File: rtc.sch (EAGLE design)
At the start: 14 parts, among them U1 MCP79412, Y1 32.768 kHz

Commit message: v1.0
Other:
- note added: "CC BY-SA"
- note added: "Jack Christensen"
- note added: "MCP79412 Breakout Board"
- note added: "MCP79412 Breakout Board by Jack Christensen is licensed under"
- note added: "a Creative Commons Attribution-ShareAlike 3.0 Unported License."
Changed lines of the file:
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@@
 <layer number="209" name="209bmp" color="7" fill="1" visible="yes" active="yes"/>
 <layer number="210" name="210bmp" color="7" fill="1" visible="yes" active="yes"/>
+<layer number="211" name="211bmp" color="7" fill="1" visible="yes" active="yes"/>
+<layer number="212" name="212bmp" color="7" fill="1" visible="yes" active="yes"/>
+<layer number="213" name="213bmp" color="7" fill="1" visible="yes" active="yes"/>
+<layer number="214" name="214bmp" color="7" fill="1" visible="yes" active="yes"/>
+<layer number="215" name="215bmp" color="7" fill="1" visible="yes" active="yes"/>
+<layer number="216" name="216bmp" color="7" fill="1" visible="yes" active="yes"/>
 <layer number="250" name="Descript" color="7" fill="1" visible="no" active="no"/>
 <layer number="251" name="SMDround" color="7" fill="1" visible="no" active="no"/>
@@
 <sheet>
 <plain>
+<text x="10.16" y="15.24" size="2.1844" layer="91" ratio="10">MCP79412 Breakout Board by Jack Christensen is licensed under</text>
+<text x="10.16" y="20.32" size="4.572" layer="91" ratio="12">CC BY-SA</text>
+<text x="10.16" y="10.16" size="2.1844" layer="91" ratio="10">a Creative Commons Attribution-ShareAlike 3.0 Unported License.</text>
+<text x="149.86" y="30.48" size="3.048" layer="91" ratio="12">MCP79412 Breakout Board</text>
+<text x="149.86" y="25.4" size="3.048" layer="91" ratio="12">Jack Christensen</text>
 </plain>
 <instances>

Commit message: v1.1 Larger pads for D1.
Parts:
- D1: device zetex:DSOD323 -> _jc:DIODESOD-323F
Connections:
- net N$1: now also D1.K; no longer D1.C
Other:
- note added: "v1.1"
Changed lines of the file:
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@@
 <layer number="109" name="fp9" color="7" fill="1" visible="yes" active="yes"/>
 <layer number="110" name="fp0" color="7" fill="1" visible="yes" active="yes"/>
+<layer number="111" name="LPC17xx" color="7" fill="1" visible="yes" active="yes"/>
+<layer number="112" name="tSilk" color="7" fill="1" visible="yes" active="yes"/>
 <layer number="116" name="Patch_BOT" color="9" fill="4" visible="yes" active="yes"/>
 <layer number="121" name="_tsilk" color="7" fill="1" visible="yes" active="yes"/>
@@
 <layer number="123" name="tTestmark" color="7" fill="1" visible="yes" active="yes"/>
 <layer number="124" name="bTestmark" color="7" fill="1" visible="yes" active="yes"/>
+<layer number="125" name="_tNames" color="7" fill="1" visible="yes" active="yes"/>
+<layer number="126" name="_bNames" color="7" fill="1" visible="yes" active="yes"/>
+<layer number="127" name="_tValues" color="7" fill="1" visible="yes" active="yes"/>
+<layer number="128" name="_bValues" color="7" fill="1" visible="yes" active="yes"/>
 <layer number="131" name="tAdjust" color="7" fill="1" visible="yes" active="yes"/>
 <layer number="132" name="bAdjust" color="7" fill="1" visible="yes" active="yes"/>
 <layer number="144" name="Drill_legend" color="7" fill="1" visible="yes" active="yes"/>
 <layer number="151" name="HeatSink" color="7" fill="1" visible="yes" active="yes"/>
+<layer number="152" name="_bDocu" color="7" fill="1" visible="yes" active="yes"/>
 <layer number="199" name="Contour" color="7" fill="1" visible="yes" active="yes"/>
 <layer number="200" name="200bmp" color="1" fill="10" visible="no" active="no"/>
@@
 <layer number="215" name="215bmp" color="7" fill="1" visible="yes" active="yes"/>
 <layer number="216" name="216bmp" color="7" fill="1" visible="yes" active="yes"/>
+<layer number="217" name="217bmp" color="7" fill="1" visible="yes" active="yes"/>
+<layer number="218" name="218bmp" color="7" fill="1" visible="yes" active="yes"/>
+<layer number="219" name="219bmp" color="7" fill="1" visible="yes" active="yes"/>
+<layer number="220" name="220bmp" color="7" fill="1" visible="yes" active="yes"/>
+<layer number="221" name="221bmp" color="7" fill="1" visible="yes" active="yes"/>
+<layer number="222" name="222bmp" color="7" fill="1" visible="yes" active="yes"/>
+<layer number="223" name="223bmp" color="7" fill="1" visible="yes" active="yes"/>
+<layer number="224" name="224bmp" color="7" fill="1" visible="yes" active="yes"/>
+<layer number="248" name="Housing" color="7" fill="1" visible="yes" active="yes"/>
+<layer number="249" name="Edge" color="7" fill="1" visible="yes" active="yes"/>
 <layer number="250" name="Descript" color="7" fill="1" visible="no" active="no"/>
 <layer number="251" name="SMDround" color="7" fill="1" visible="no" active="no"/>
@@
 <part name="GND5" library="supply1" deviceset="GND" device=""/>
 <part name="P+2" library="supply1" deviceset="VCC" device=""/>
-<part name="D1" library="zetex" deviceset="D" device="SOD323" value="PMEG6002EJ"/>
+<part name="D1" library="_jc" deviceset="DIODE" device="SOD-323F" value="PMEG6002EJ"/>
 <part name="B1" library="_jc" deviceset="COIN-CELL" device="-2016-SMT" value="CR2016"/>
 <part name="GND6" library="supply1" deviceset="GND" device=""/>
@@
 <text x="149.86" y="30.48" size="3.048" layer="91" ratio="12">MCP79412 Breakout Board</text>
 <text x="149.86" y="25.4" size="3.048" layer="91" ratio="12">Jack Christensen</text>
+<text x="236.22" y="7.62" size="3.048" layer="91" ratio="12">v1.1</text>
 </plain>
 <instances>
@@
 <segment>
 <pinref part="R4" gate="G$1" pin="2"/>
-<pinref part="D1" gate="G$1" pin="C"/>
+<pinref part="D1" gate="G$1" pin="K"/>
 <wire x1="81.28" y1="83.82" x2="78.74" y2="83.82" width="0.1524" layer="91"/>
 </segment>

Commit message: Updated coin cell footprint, R and C footprints, OSHW logo.
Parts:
- added LOGO2: OSHW_LOGO_8MILX0150-NT, ohw-logo:OSHW_LOGO_8MILX0150-NT
- C1, C2, C3, C4: device rcl:C-USC0805 -> _jc:C-USM0805
- R1, R2, R3, R4: device rcl:R-US_R0805 -> _jc:R-US_M0805
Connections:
- net BAT: now also B1.POS1, B1.POS2; no longer B1.B+
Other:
- note added: "v1.2"
- note removed: "v1.1"
- moved on the sheet: C2, C3, C4, D1, R4, Y1

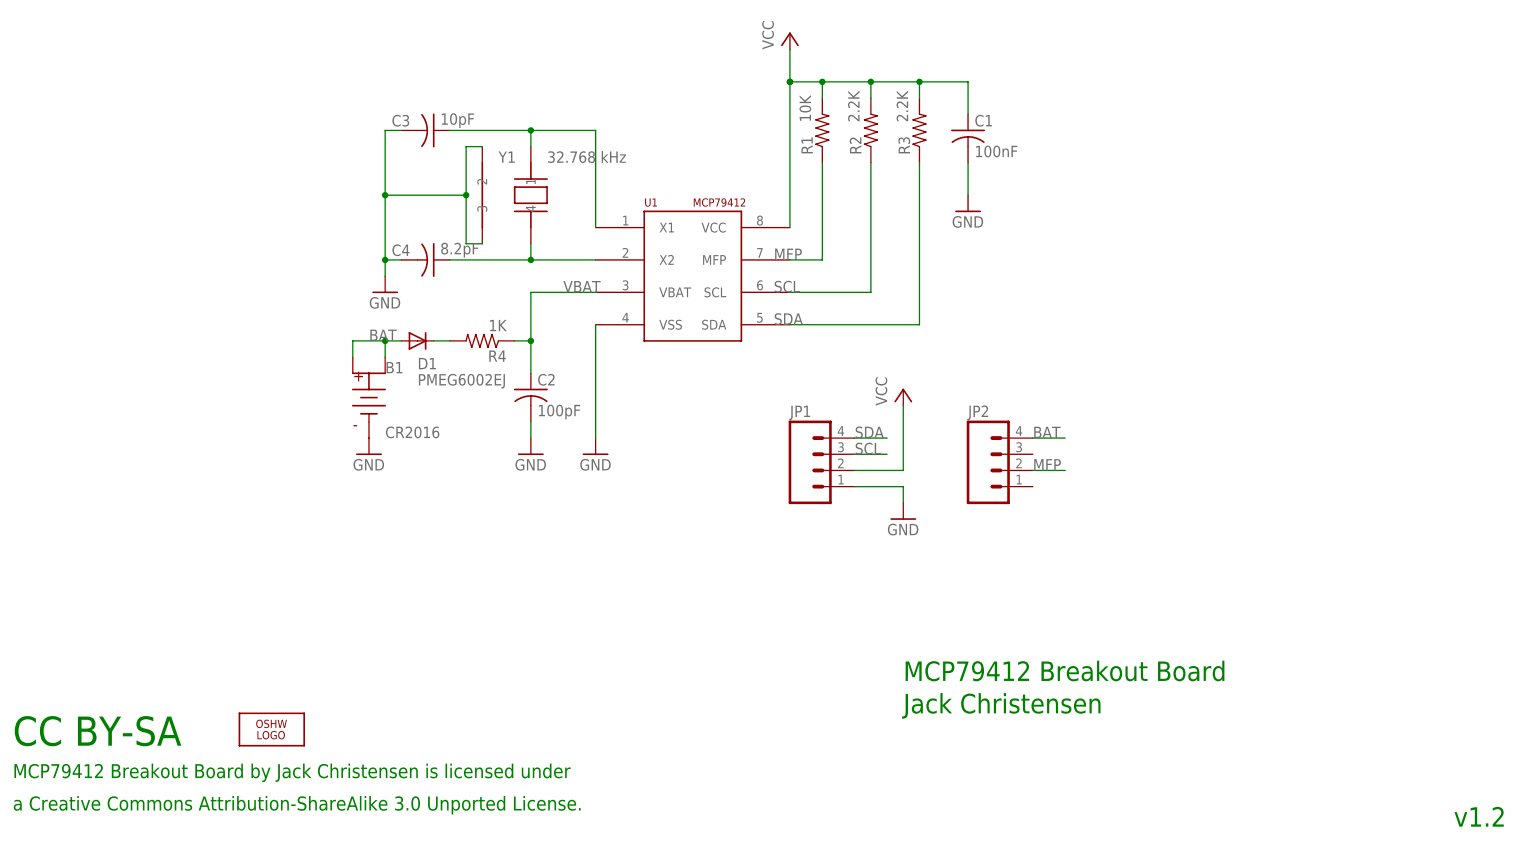
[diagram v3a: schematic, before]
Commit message: Update README, add LICENSE and other misc files. Regenerate Gerber files.
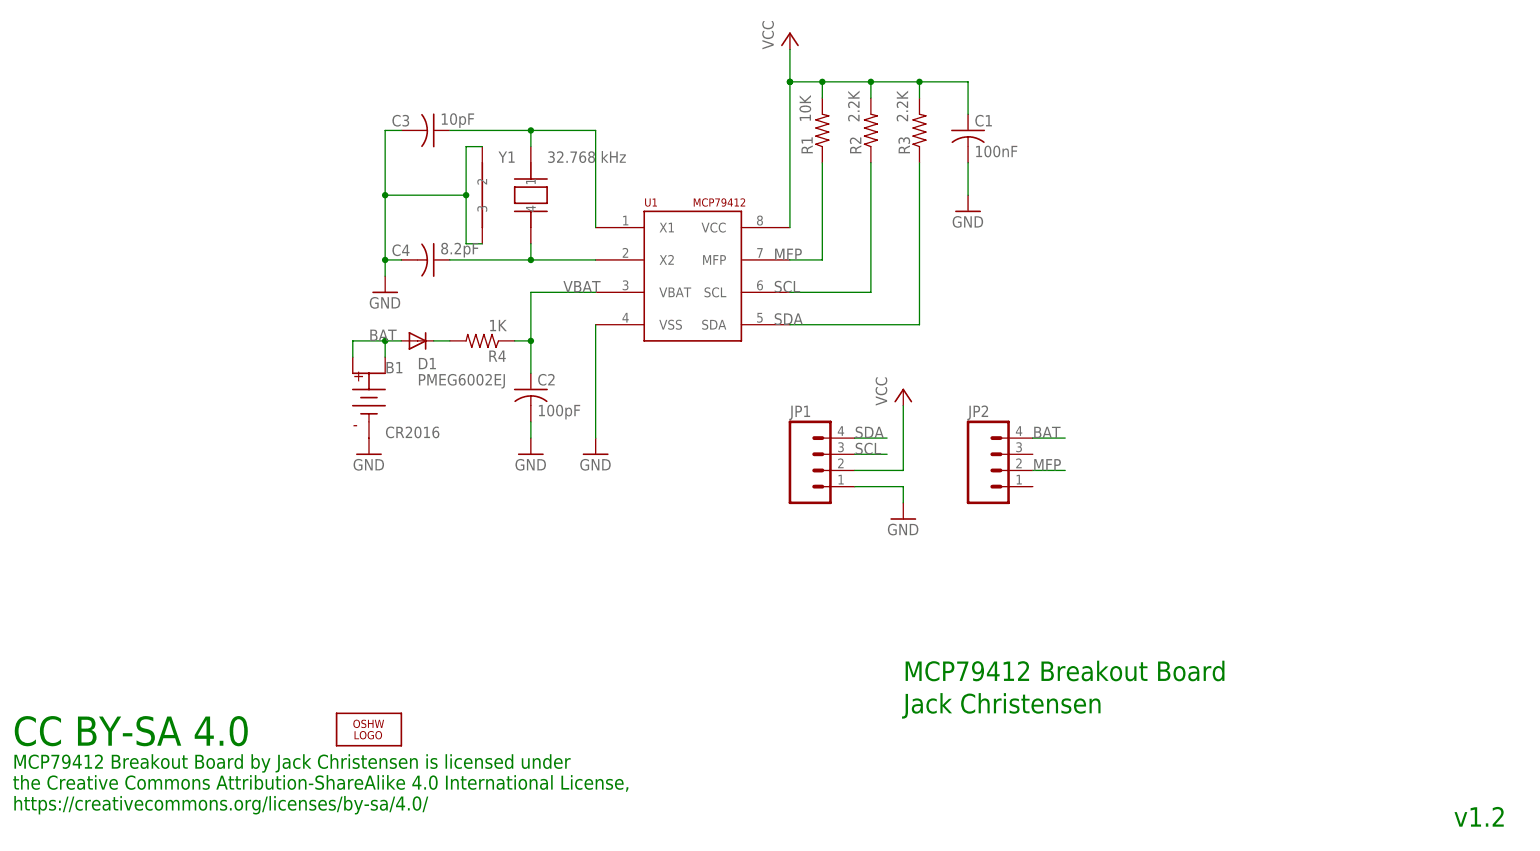
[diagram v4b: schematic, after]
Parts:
- D1: device _jc:DIODESOD-323F -> _jc:DIODESOD-323F-A
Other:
- note added: "CC BY-SA 4.0"
- note added: "MCP79412 Breakout Board by Jack Christensen is licensed under the Creative Commons Attribution-ShareAlike 4.0 International License, https://creativecommons.org/licenses/by-sa/4.0/"
- note removed: "CC BY-SA"
- note removed: "MCP79412 Breakout Board by Jack Christensen is licensed under"
- note removed: "a Creative Commons Attribution-ShareAlike 3.0 Unported License."
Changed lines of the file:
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@@
 <?xml version="1.0" encoding="utf-8"?>
 <!DOCTYPE eagle SYSTEM "eagle.dtd">
-<eagle version="6.4">
+<eagle version="9.6.2">
 <drawing>
 <settings>
 <setting alwaysvectorfont="yes"/>
+<setting keepoldvectorfont="yes"/>
 <setting verticaltext="up"/>
 </settings>
@@
 <layer number="97" name="Info" color="7" fill="1" visible="yes" active="yes"/>
 <layer number="98" name="Guide" color="6" fill="1" visible="yes" active="yes"/>
+<layer number="99" name="SpiceOrder" color="5" fill="1" visible="no" active="no"/>
 <layer number="100" name="Muster" color="7" fill="1" visible="no" active="no"/>
 <layer number="101" name="Patch_Top" color="12" fill="4" visible="yes" active="yes"/>
@@
 <part name="GND5" library="supply1" deviceset="GND" device=""/>
 <part name="P+2" library="supply1" deviceset="VCC" device=""/>
-<part name="D1" library="_jc" deviceset="DIODE" device="SOD-323F" value="PMEG6002EJ"/>
+<part name="D1" library="_jc" deviceset="DIODE" device="SOD-323F-A" value="PMEG6002EJ"/>
 <part name="GND6" library="supply1" deviceset="GND" device=""/>
 <part name="Y1" library="_jc" deviceset="CRYSTAL-CITIZEN-CM2XXC" device="" value="32.768 kHz"/>
@@
 <sheet>
 <plain>
-<text x="10.16" y="15.24" size="2.1844" layer="91" ratio="10">MCP79412 Breakout Board by Jack Christensen is licensed under</text>
-<text x="10.16" y="20.32" size="4.572" layer="91" ratio="12">CC BY-SA</text>
-<text x="10.16" y="10.16" size="2.1844" layer="91" ratio="10">a Creative Commons Attribution-ShareAlike 3.0 Unported License.</text>
+<text x="10.16" y="10.16" size="2.1844" layer="91" ratio="10">MCP79412 Breakout Board by Jack Christensen is licensed under
+the Creative Commons Attribution-ShareAlike 4.0 International License,
+https://creativecommons.org/licenses/by-sa/4.0/</text>
+<text x="10.16" y="20.32" size="4.572" layer="91" ratio="12">CC BY-SA 4.0</text>
 <text x="149.86" y="30.48" size="3.048" layer="91" ratio="12">MCP79412 Breakout Board</text>
 <text x="149.86" y="25.4" size="3.048" layer="91" ratio="12">Jack Christensen</text>
@@
 </plain>
 <instances>
-<instance part="FRAME1" gate="G$1" x="0" y="0"/>
-<instance part="FRAME1" gate="G$2" x="147.32" y="0"/>
+<instance part="FRAME1" gate="G$1" x="0" y="0" smashed="yes"/>
+<instance part="FRAME1" gate="G$2" x="147.32" y="0" smashed="yes">
+<attribute name="LAST_DATE_TIME" x="160.02" y="1.27" size="2.54" layer="94" font="vector"/>
+<attribute name="SHEET" x="233.68" y="1.27" size="2.54" layer="94" font="vector"/>
+<attribute name="DRAWING_NAME" x="165.1" y="19.05" size="2.54" layer="94" font="vector"/>
+</instance>
 <instance part="U1" gate="G$1" x="116.84" y="93.98" smashed="yes">
 <attribute name="NAME" x="109.22" y="104.902" size="1.27" layer="94"/>
@@
 <attribute name="VALUE" x="93.98" y="111.76" size="1.778" layer="96"/>
 </instance>
-<instance part="B1" gate="G$1" x="66.04" y="73.66"/>
-<instance part="LOGO2" gate="G$1" x="50.8" y="22.86"/>
+<instance part="B1" gate="G$1" x="66.04" y="73.66" smashed="yes">
+<attribute name="NAME" x="68.58" y="78.74" size="1.778" layer="95"/>
+<attribute name="VALUE" x="68.58" y="68.58" size="1.778" layer="96"/>
+</instance>
+<instance part="LOGO2" gate="G$1" x="66.04" y="22.86" smashed="yes"/>
 </instances>
 <busses>
@@
 </schematic>
 </drawing>
+<compatibility>
+<note version="6.3" minversion="6.2.2" severity="warning">
+Since Version 6.2.2 text objects can contain more than one line,
+which will not be processed correctly with this version.
+</note>
+</compatibility>
 </eagle>
